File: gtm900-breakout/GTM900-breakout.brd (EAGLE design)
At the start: 70.2 x 100 mm, 118 parts, among them IC1 SN74AVC4T245-VQFN, IC2 NAU88C10, IC3 TXB0102, J1 AUDIO-JACK3, K1 PJ-002BH-SMT-TR, T1 BC847, T2 BC847, U1 FH12A-40S-0.5SH(55), U2 MIC5366, U3 MCP1827T-ADJE/ET, U4 RASPBERRY_PICOSMD

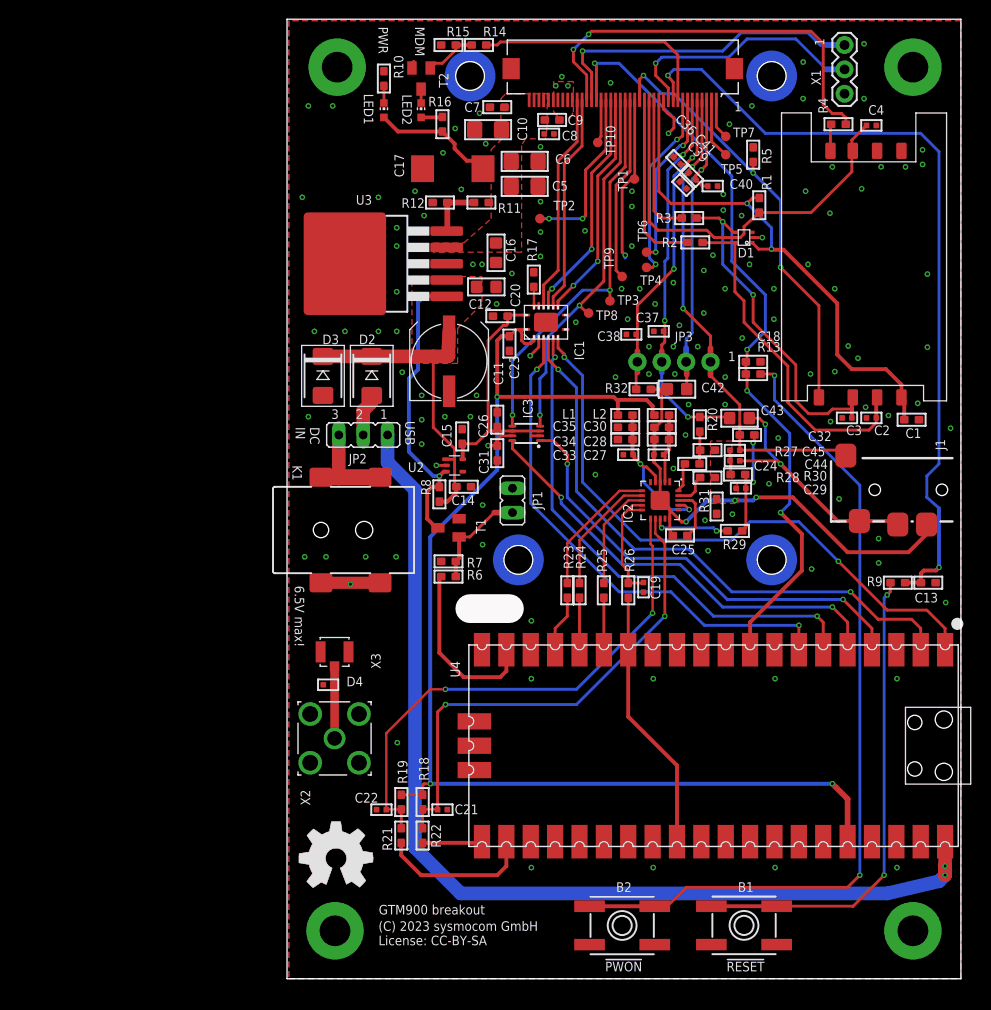
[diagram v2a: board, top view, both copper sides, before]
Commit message: gtm900-bo: switch direction inputs for level shifter IC1
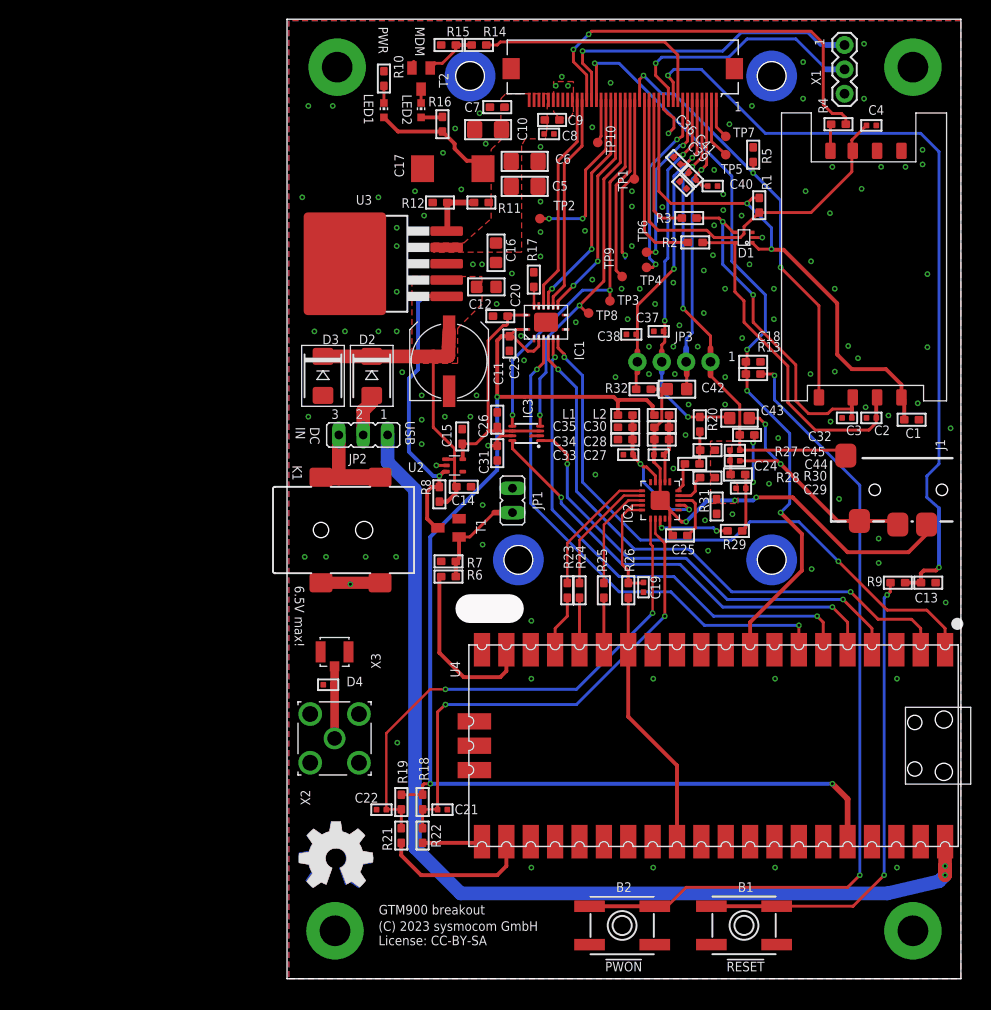
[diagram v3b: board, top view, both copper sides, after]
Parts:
- added U$1: (no value), oshw:OSHW_8MM_COPPER
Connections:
- net GND: now also IC1.2; no longer IC1.3
- net VCC: now also IC1.3; no longer IC1.2
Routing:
- net GND: track 16.3 -> 14.1 mm, vias 135 -> 141
- net VCC: track 131.9 -> 133.6 mm
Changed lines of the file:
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@@
 <layer number="24" name="bOrigins" color="15" fill="1" visible="yes" active="yes"/>
 <layer number="25" name="tNames" color="7" fill="1" visible="yes" active="yes"/>
-<layer number="26" name="bNames" color="7" fill="1" visible="yes" active="yes"/>
+<layer number="26" name="bNames" color="7" fill="1" visible="no" active="yes"/>
 <layer number="27" name="tValues" color="7" fill="1" visible="no" active="yes"/>
 <layer number="28" name="bValues" color="7" fill="1" visible="no" active="yes"/>
-<layer number="29" name="tStop" color="7" fill="3" visible="no" active="yes"/>
+<layer number="29" name="tStop" color="7" fill="3" visible="yes" active="yes"/>
 <layer number="30" name="bStop" color="7" fill="6" visible="no" active="yes"/>
 <layer number="31" name="tCream" color="7" fill="4" visible="no" active="yes"/>
@@
 <layer number="37" name="tTest" color="7" fill="1" visible="no" active="yes"/>
 <layer number="38" name="bTest" color="7" fill="1" visible="no" active="yes"/>
-<layer number="39" name="tKeepout" color="4" fill="11" visible="no" active="yes"/>
-<layer number="40" name="bKeepout" color="1" fill="11" visible="no" active="yes"/>
-<layer number="41" name="tRestrict" color="4" fill="10" visible="no" active="yes"/>
-<layer number="42" name="bRestrict" color="1" fill="10" visible="no" active="yes"/>
-<layer number="43" name="vRestrict" color="2" fill="10" visible="no" active="yes"/>
+<layer number="39" name="tKeepout" color="4" fill="11" visible="yes" active="yes"/>
+<layer number="40" name="bKeepout" color="1" fill="11" visible="yes" active="yes"/>
+<layer number="41" name="tRestrict" color="4" fill="10" visible="yes" active="yes"/>
+<layer number="42" name="bRestrict" color="1" fill="10" visible="yes" active="yes"/>
+<layer number="43" name="vRestrict" color="2" fill="10" visible="yes" active="yes"/>
 <layer number="44" name="Drills" color="7" fill="1" visible="no" active="yes"/>
 <layer number="45" name="Holes" color="7" fill="1" visible="no" active="yes"/>
-<layer number="46" name="Milling" color="3" fill="1" visible="yes" active="yes"/>
+<layer number="46" name="Milling" color="3" fill="1" visible="no" active="yes"/>
 <layer number="47" name="Measures" color="7" fill="1" visible="no" active="yes"/>
 <layer number="48" name="Document" color="7" fill="1" visible="yes" active="yes"/>
@@
 <wire x1="0" y1="100" x2="70.2285" y2="100" width="0" layer="20"/>
 <wire x1="70.2285" y1="100" x2="70.2285" y2="0" width="0" layer="20"/>
-<text x="62.0395" y="76.482" size="1" layer="26" font="vector" ratio="16" rot="SMR270">GTM900 breakout</text>
-<text x="65.3415" y="82.832" size="1" layer="26" font="vector" ratio="16" rot="SMR270">(C) 2023 sysmocom GmbH
+<text x="29.1745" y="5.9055" size="1" layer="26" font="vector" ratio="16" rot="SMR0">GTM900 breakout</text>
+<text x="29.1745" y="2.6035" size="1" layer="26" font="vector" ratio="16" rot="SMR0">(C) 2023 sysmocom GmbH
 License: CC-BY-SA</text>
-<text x="62.0395" y="79.403" size="1" layer="26" font="vector" ratio="16" rot="SMR270">&gt;VERSION</text>
+<text x="15.268" y="5.9055" size="1" layer="26" font="vector" ratio="16" rot="SMR0">&gt;VERSION</text>
 <text x="47.3825" y="91.398" size="1" layer="21" font="vector" ratio="16" rot="R180">1</text>
 <text x="0.889" y="57.4955" size="1" layer="25" font="vector" ratio="16" rot="SR270">DC
@@
 <attribute name="VALUE" x="48.5775" y="52.4511" size="0.508" layer="27" font="vector" ratio="10" rot="R180"/>
 </element>
+<element name="U$1" library="oshw" package="OSHW_8MM_COPPER" value="" x="5.08" y="12.5375" smashed="yes" rot="MR0"/>
 </elements>
 <signals>
@@
 <via x="59.4995" y="64.671" extent="1-16" drill="0.3"/>
 <via x="57.0865" y="63.274" extent="1-16" drill="0.3"/>
-<via x="54.2925" y="74.45" extent="1-16" drill="0.3"/>
+<via x="54.61" y="74.7675" extent="1-16" drill="0.3"/>
 <via x="57.0865" y="71.91" extent="1-16" drill="0.3"/>
 <via x="66.2305" y="86.388" extent="1-16" drill="0.3"/>
@@
 <via x="14.0335" y="55.7175" extent="1-16" drill="0.3"/>
 <contactref element="IC1" pad="9"/>
-<contactref element="IC1" pad="3"/>
 <contactref element="IC1" pad="8"/>
 <contactref element="C23" pad="1"/>
@@
 <wire x1="26.3775" y1="56.5825" x2="25.4675" y2="56.5825" width="0.3048" layer="1"/>
 <wire x1="25.4675" y1="56.5825" x2="25.4" y2="56.515" width="0.3048" layer="1"/>
-<via x="25.3365" y="64.925" extent="1-16" drill="0.3"/>
-<wire x1="26.2375" y1="66.7175" x2="26.2375" y2="65.826" width="0.3048" layer="1"/>
-<wire x1="26.2375" y1="65.826" x2="25.3365" y2="64.925" width="0.3048" layer="1"/>
 <via x="30.099" y="68.4175" extent="1-16" drill="0.3"/>
 <via x="46.4185" y="48.415" extent="1-16" drill="0.3"/>
@@
 <via x="40.259" y="65.8775" extent="1-16" drill="0.3"/>
 <via x="38.354" y="70.3225" extent="1-16" drill="0.3"/>
+<via x="39.116" y="80.4175" extent="1-16" drill="0.3"/>
+<via x="44.5135" y="78.5125" extent="1-16" drill="0.3"/>
+<via x="44.5135" y="84.2925" extent="1-16" drill="0.3"/>
+<via x="31.8135" y="88.7375" extent="1-16" drill="0.3"/>
+<via x="31.8135" y="72.8625" extent="1-16" drill="0.3"/>
+<contactref element="IC1" pad="2"/>
+<via x="24.384" y="66.98875" extent="1-16" drill="0.3"/>
+<via x="24.7015" y="64.44875" extent="1-16" drill="0.3"/>
 </signal>
 <signal name="USIM_CLK">
@@
 <contactref element="C23" pad="2"/>
 <contactref element="IC1" pad="1"/>
-<contactref element="IC1" pad="2"/>
 <contactref element="C31" pad="2"/>
 <contactref element="IC3" pad="7"/>
 <contactref element="R18" pad="2"/>
 <contactref element="R19" pad="2"/>
-<wire x1="24.89625" y1="67.6675" x2="24.13" y2="67.6675" width="0.3048" layer="1"/>
-<wire x1="24.13" y1="67.6675" x2="23.888" y2="67.6675" width="0.3048" layer="1"/>
+<wire x1="24.89625" y1="67.6675" x2="23.888" y2="67.6675" width="0.3048" layer="1"/>
 <wire x1="23.888" y1="67.6675" x2="23.1775" y2="66.957" width="0.3048" layer="1"/>
-<wire x1="25.7375" y1="66.7175" x2="25.7375" y2="66.5325" width="0.3048" layer="1"/>
-<wire x1="25.7375" y1="66.5325" x2="25.4" y2="66.195" width="0.3048" layer="1"/>
-<wire x1="25.4" y1="66.195" x2="24.765" y2="66.195" width="0.3048" layer="1"/>
-<wire x1="24.765" y1="66.195" x2="24.4475" y2="66.5125" width="0.3048" layer="1"/>
-<wire x1="24.4475" y1="66.5125" x2="24.4475" y2="67.35" width="0.3048" layer="1"/>
-<wire x1="24.4475" y1="67.35" x2="24.13" y2="67.6675" width="0.3048" layer="1"/>
 <wire x1="21.9075" y1="60.6425" x2="21.9075" y2="60.63875" width="0.4064" layer="1"/>
 <wire x1="21.9075" y1="60.63875" x2="21.9075" y2="66.5125" width="0.4064" layer="1"/>
@@
 <wire x1="34.4805" y1="60.198" x2="34.6075" y2="60.325" width="0.4064" layer="1"/>
 <wire x1="34.036" y1="60.6425" x2="34.4805" y2="60.198" width="0.4064" layer="1"/>
+<contactref element="IC1" pad="3"/>
+<wire x1="26.2375" y1="66.7175" x2="26.2375" y2="65.925" width="0.3048" layer="1"/>
+<wire x1="26.2375" y1="65.925" x2="25.7175" y2="65.405" width="0.3048" layer="1"/>
+<wire x1="25.7175" y1="65.405" x2="25.0825" y2="65.405" width="0.3048" layer="1"/>
+<wire x1="25.0825" y1="65.405" x2="23.5305" y2="66.957" width="0.3048" layer="1"/>
+<wire x1="23.1775" y1="66.957" x2="23.5305" y2="66.957" width="0.3048" layer="1"/>
 </signal>
 <signal name="SPKOUT+">

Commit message: gtm900-bo: add 47R into both UARTs' wires
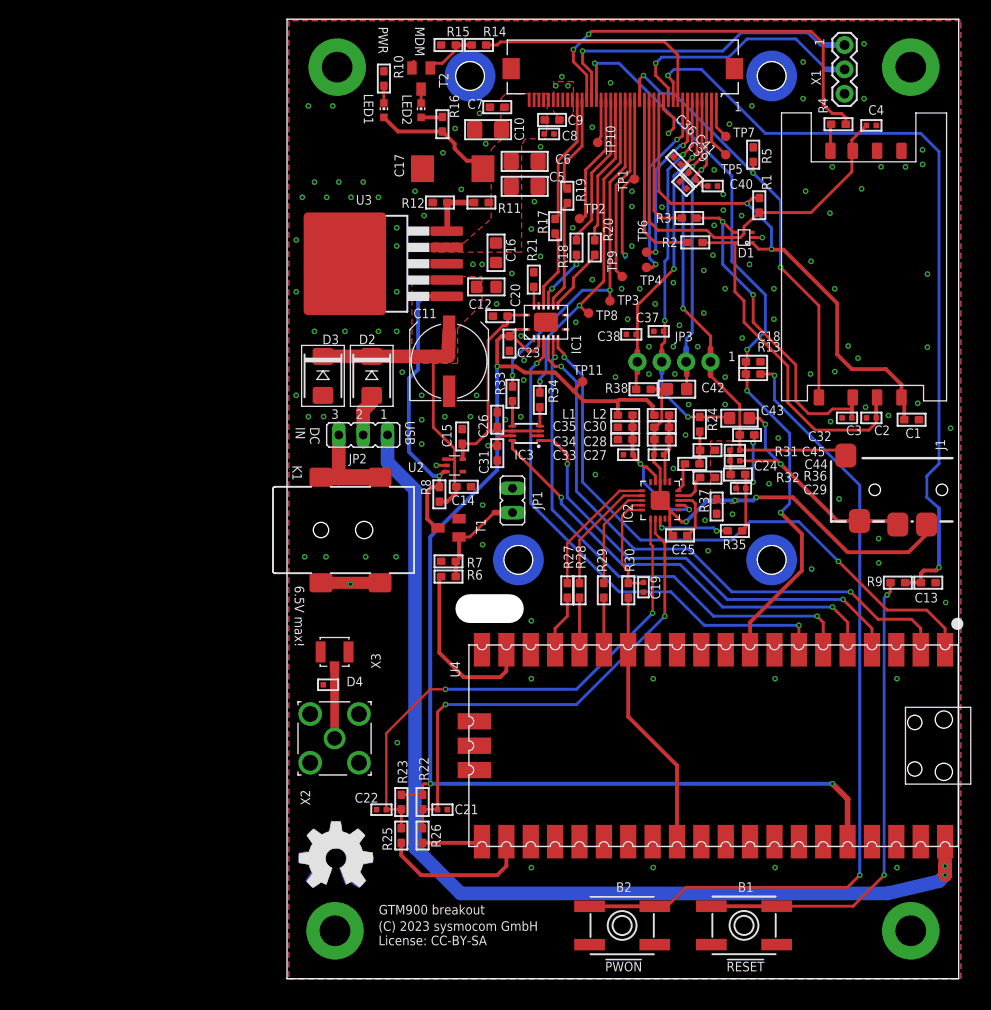
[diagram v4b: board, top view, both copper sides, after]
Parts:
- added R33, R34: 47, rc-sysmocom:_0603
- added R35: 22k, rc-sysmocom:_0603
- added R36: 1k, rc-sysmocom:_0603
- added R37, R38: 0, rc-sysmocom:_0603
- added TP11: TPTP10R, testpad:TP10R
- B1, B2: value (none) -> EVQ-Q2M03W
- R17: value 0 -> 47
- R18, R19: value 4,7k -> 47
- R20: value 22k -> 47
- R21: value 220 -> 0
- R22, R23: value 220 -> 4.7k
- R24: value 220 -> 22k
- R27, R28, R30: value 1k -> 220
- R29: value 22k -> 220
- R31, R32: value 0 -> 1k
- moved R19 65.5 mm to (29.2, 81.6)
- moved R18 60.0 mm to (30.2, 76.2)
- moved R21 59.6 mm to (25.7, 72.9), turned to 90 degrees
- moved R26 33.4 mm to (14.1, 14.9)
- moved R25 33.2 mm to (11.9, 14.9)
- moved R23 28.0 mm to (11.9, 18.4), turned to 90 degrees
- moved R20 21.4 mm to (32.1, 76.2), turned to 90 degrees
- moved R24 21.4 mm to (43.0, 57.8)
- moved R27 20.7 mm to (29.2, 40.5), turned to 270 degrees
- moved R28 17.8 mm to (30.5, 40.5), turned to 270 degrees
- moved R30 16.6 mm to (35.6, 40.5), turned to 270 degrees
- moved R29 15.0 mm to (33.0, 40.5), turned to 270 degrees
- moved R32 11.4 mm to (43.8, 52.2), turned to 0 degrees
- moved R17 5.99 mm to (27.9, 78.4)
- moved R31 5.95 mm to (43.8, 55.1), turned to 0 degrees
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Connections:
- removed net SPKOUT+: IC2.14
- removed net SPKOUT-: IC2.16
- removed net SWGND: U4.P$42
- new net N$23: IC1.13, R17.1
- new net N$27: IC1.12, R18.1
- new net N$29: IC1.11, R19.1
- new net N$32: IC1.10, R20.1
- new net N$33: IC3.5, R33.1
- new net N$34: IC3.4, R34.1
- net AGND: now also R31.2, R32.2, R36.2, R37.1, R38.1; no longer R27.2, R28.2, R30.2, R31.1, R32.1
- net EAR+: now also R24.1; no longer R20.1
- net EAR-: now also R38.2; no longer R32.2
- net GND: now also R21.2, R37.2, U4.P$42; no longer R17.2, R31.2
- net N$11: now also R30.1; no longer R26.1
- net N$12: now also R29.1; no longer R25.1
- net N$14: now also R28.1; no longer R24.1
- net N$15: now also R27.1; no longer R23.1
- net N$16: now also R35.2, R36.1; no longer R29.2, R30.1
- net N$18: now also R32.1; no longer R28.1
- net N$22: now also R21.1; no longer R17.1
- net N$25: now also R26.1; no longer R18.1
- net N$26: now also R23.1, R25.1; no longer R19.1, R21.1
- net N$30: now also R35.1; no longer R29.1
- net N$7: now also R24.2, R31.1; no longer R20.2, R27.1
- net PCM_CLK_RP2: now also R30.2; no longer R26.2
- net PCM_FRAME_RP2: now also R29.2; no longer R25.2
- net PCM_MISO_RP2: now also R27.2; no longer R23.2
- net PCM_MOSI_RP2: now also R28.2; no longer R24.2
- net RXD2: now also R17.2; no longer IC1.13
- net SCL: now also R25.2; no longer R21.2
- net SDA: now also R26.2; no longer R22.2
- net TXD2: now also R19.2; no longer IC1.11
- net UART_CTS: now also R34.2; no longer IC3.4
- net UART_RTS: now also R33.2; no longer IC3.5
- net UART_RXD: now also R18.2; no longer IC1.12
- net UART_TXD: now also R20.2; no longer IC1.10
- net VCC: now also R22.2, R23.2, TP11.TP; no longer R18.2, R19.2
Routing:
- net TXD2: track 22.7 -> 10.3 mm
- net N$29: track 0.00 -> 11.3 mm
- net RXD2: track 22.9 -> 13.4 mm
- net UART_TXD: track 24.0 -> 15.5 mm, vias 2 -> 0
- net N$23: track 0.00 -> 8.30 mm
- net UART_RXD: track 24.2 -> 16.1 mm, vias 2 -> 0
- net N$32: track 0.00 -> 6.91 mm
- net N$27: track 0.00 -> 6.53 mm, vias 0 -> 2
- net UART_RTS: track 41.7 -> 37.5 mm
- net UART_RI: track 17.8 -> 13.7 mm, vias 2 -> 0
- net UART_CTS: track 38.8 -> 35.3 mm
- net N$33: track 0.00 -> 2.62 mm
- net VCC: track 133.6 -> 136.1 mm
- net N$34: track 0.00 -> 1.99 mm
- net GND: vias 141 -> 153
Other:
- board size 70.2 x 100 mm -> 70 x 100 mm
